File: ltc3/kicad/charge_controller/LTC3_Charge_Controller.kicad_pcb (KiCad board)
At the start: 4 copper layers, 102 x 83 mm, 394 parts, among them P1 MicroFit header, P2 MicroFit header, P3 JST XH header, P4 MicroFit header, P5 JST XH header, P6 JST XH header, Q1 ZVN4525E6, Q2 BSC028N06NS, Q3 BSC028N06NS, Q4 BSC028N06NS, Q5 BSC028N06NS, Q6 ZVP3310F, Q7 MMBT5550L, U1 PI2127, U2 PI2127, U3 LT8490, U4 LTC2990

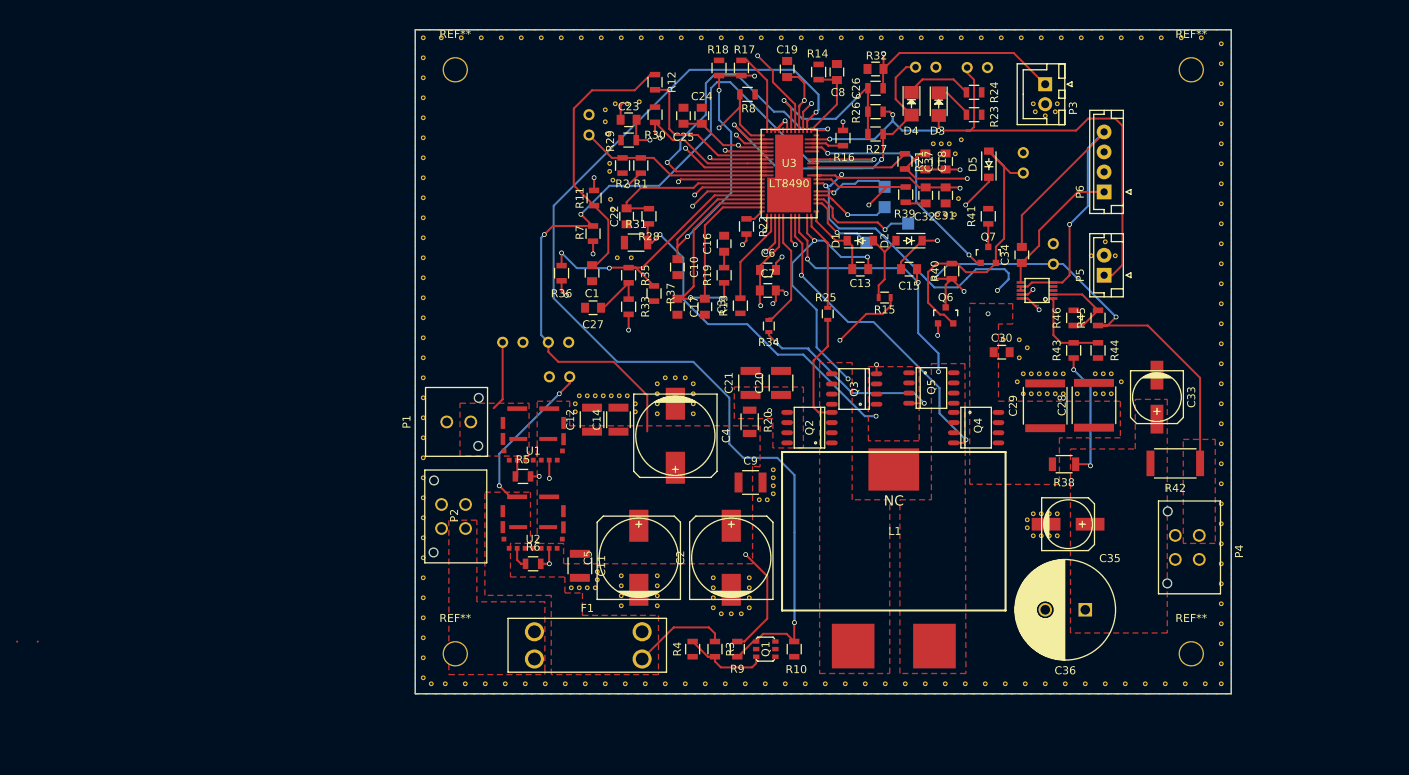
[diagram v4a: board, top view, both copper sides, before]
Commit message: LTC3 Layout Changes to Charge Controller/Cell Balancing
Finished up some changes on charge controller/cell balancing layout.
DRC gives zero errors, and everything is connected, huzzah!
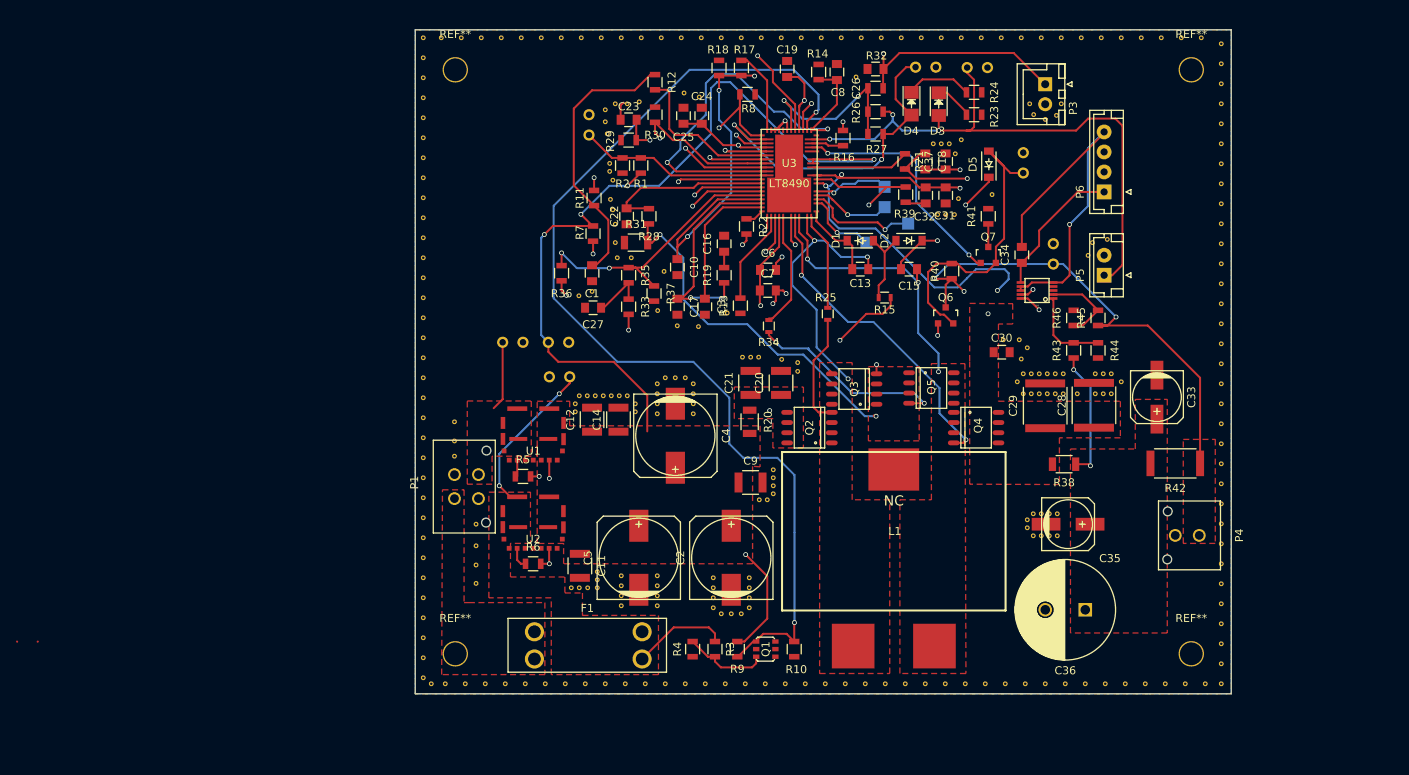
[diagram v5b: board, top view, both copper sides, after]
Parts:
- removed P2: MicroFit header, Connectors_Molex:Molex_Microfit3_Header_02x02_Straight_43045-0428
- removed the REF** at (171.2, 136.0)
- added REF**: Via_.6mm, LTC3:Via_.6mm, F.Cu at (164.6, 82.4)
- added REF**: Via_.6mm, LTC3:Via_.6mm, F.Cu at (122.8, 96.9)
- added REF**: Via_.6mm, LTC3:Via_.6mm, F.Cu at (125.2, 98.8)
- added REF**: Via_.6mm, LTC3:Via_.6mm, F.Cu at (127.9, 98.9)
- added REF**: Via_.6mm, LTC3:Via_.6mm, F.Cu at (131.5, 97.2)
- added REF**: Via_.6mm, LTC3:Via_.6mm, F.Cu at (138.3, 103.0)
- added REF**: Via_.6mm, LTC3:Via_.6mm, F.Cu at (140.3, 103.4)
- added REF**: Via_.6mm, LTC3:Via_.6mm, F.Cu at (140.3, 104.5)
- added REF**: Via_.6mm, LTC3:Via_.6mm, F.Cu at (133.4, 102.7)
- added REF**: Via_.6mm, LTC3:Via_.6mm, F.Cu at (135.4, 102.7)
- added REF**: Via_.6mm, LTC3:Via_.6mm, F.Cu at (134.4, 102.7)
- added REF**: Via_.6mm, LTC3:Via_.6mm, F.Cu at (147.6, 67.7)
- added REF**: Via_.6mm, LTC3:Via_.6mm, F.Cu at (97.4, 110.8)
- added REF**: Via_.6mm, LTC3:Via_.6mm, F.Cu at (97.4, 113.2)
- added REF**: Via_.6mm, LTC3:Via_.6mm, F.Cu at (97.4, 115.1)
- added REF**: Via_.6mm, LTC3:Via_.6mm, F.Cu at (100.1, 123.6)
- added REF**: Via_.6mm, LTC3:Via_.6mm, F.Cu at (100.1, 131.0)
- added REF**: Via_.6mm, LTC3:Via_.6mm, F.Cu at (100.1, 128.7)
- added REF**: Via_.6mm, LTC3:Via_.6mm, F.Cu at (100.1, 126.3)
- added REF**: Via_.6mm, LTC3:Via_.6mm, F.Cu at (128.0, 70.2)
- added REF**: Via_.6mm, LTC3:Via_.6mm, F.Cu at (126.1, 69.7)
- added REF**: Via_.6mm, LTC3:Via_.6mm, F.Cu at (123.6, 92.0)
- added REF**: Via_.6mm, LTC3:Via_.6mm, F.Cu at (117.5, 88.4)
- added REF**: Via_.6mm, LTC3:Via_.6mm, F.Cu at (117.5, 86.1)
- added REF**: Via_.6mm, LTC3:Via_.6mm, F.Cu at (114.6, 94.5)
- added REF**: Via_.6mm, LTC3:Via_.6mm, F.Cu at (171.3, 136.2)
- added REF**: Via_.6mm, LTC3:Via_.6mm, F.Cu at (112.9, 95.0)
- C1: value 0.33u -> 0.33μ
- C10, C8: value 0.01u -> 0.01μ
- C11, C12, C14, C20, C21, C9: value 2.2u -> 2.2μ
- C2, C4, C5: value 33u -> 33μ
- C22, C23: value 0.001u -> 0.001μ
- C24, C28, C29, C6, C7: value 4.7u -> 4.7μ
- C25, C30: value 1u -> 1μ
- C26, C3, C31, C34, C37: value 0.1u -> 0.1μ
- C27: value 0.18u -> 0.18μ
- C33, C35: value 10u -> 10μ
- C36: value 150u -> 150μ
- P1: footprint Connectors_Molex:Molex_Microfit3_Header_02x01_Straight_43045-0228 -> Connectors_Molex:Molex_Microfit3_Header_02x02_Straight_43045-0428
- P3, P5, P6: value JST XH header -> XH header
- P4: footprint Connectors_Molex:Molex_Microfit3_Header_02x02_Straight_43045-0428 -> Connectors_Molex:Molex_Microfit3_Header_02x01_Straight_43045-0228
- moved P1 9.63 mm to (97.4, 120.4)
- moved REF** 3.29 mm to (177.1, 88.4)
- moved REF** 0.50 mm to (173.2, 71.0)
- moved REF** 0.47 mm to (172.6, 72.5)
- moved REF** 0.45 mm to (173.2, 134.2)
- moved REF** 0.45 mm to (171.2, 132.3)
- moved REF** 0.45 mm to (171.2, 73.0)
- moved REF** 0.45 mm to (169.3, 71.0)
- moved REF** 0.45 mm to (169.3, 134.3)
- moved REF** 0.40 mm to (169.8, 72.4)
- moved REF** 0.40 mm to (176.6, 90.0)
- moved REF** 0.39 mm to (179.0, 88.0)
- moved REF** 0.29 mm to (168.2, 102.9)
- moved REF** 0.25 mm to (172.7, 132.9)
- moved REF** 0.25 mm to (115.2, 131.5)
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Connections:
- F1 pad 1: Net-(F1-Pad1) -> /LAB_IN
- P1 pad 1: GND -> /LAB_IN
- P1 pad 2: Net-(P1-Pad2) -> GND
- U1 pad 12: Net-(P1-Pad2) -> /PV_IN
- U1 pad 13: Net-(P1-Pad2) -> /PV_IN
- U1 pad 14: Net-(P1-Pad2) -> /PV_IN
- U1 pad 15: Net-(P1-Pad2) -> /PV_IN
- U1 pad 16: Net-(P1-Pad2) -> /PV_IN
- W3 pad 1: Net-(P1-Pad2) -> /PV_IN
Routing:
- net Net-(P1-Pad2): track 8.70 -> 0.00 mm
- net /PV_IN: track 0.00 -> 8.70 mm
- added copper zone on F.Cu, net /LAB_IN
- added copper zone on F.Cu, net /PV_IN
- removed copper zone on F.Cu, net Net-(F1-Pad1)
- removed copper zone on F.Cu, net Net-(P1-Pad2)

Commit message: LTC3 Layout
Minor changes to charge controller PCB.
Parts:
- added REF**: Via_.6mm, LTC3:Via_.6mm, F.Cu at (164.7, 72.8)
- added REF**: Via_.6mm, LTC3:Via_.6mm, F.Cu at (164.7, 71.8)
- added REF**: Via_.6mm, LTC3:Via_.6mm, F.Cu at (164.7, 70.2)
- added REF**: Via_.6mm, LTC3:Via_.6mm, F.Cu at (164.7, 69.1)
- added REF**: Via_.6mm, LTC3:Via_.6mm, F.Cu at (186.9, 103.4)
- added REF**: Via_.6mm, LTC3:Via_.6mm, F.Cu at (183.3, 103.4)
- added REF**: Via_.6mm, LTC3:Via_.6mm, F.Cu at (186.9, 104.9)
- added REF**: Via_.6mm, LTC3:Via_.6mm, F.Cu at (185.2, 102.0)
- added REF**: Via_.6mm, LTC3:Via_.6mm, F.Cu at (183.3, 104.9)
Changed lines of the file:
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@@
 (kicad_pcb (version 4) (host pcbnew "(2016-05-27 BZR 6836, Git 4441a4b)-product")
   (general
-    (links 572)
+    (links 581)
     (no_connects 0)
-    (area 92.405999 61.725999 194.506001 144.826001)
+    (area 42.423199 60.5199 199.831029 145.9171)
     (thickness 1.6)
     (drawings 4)
     (tracks 824)
     (zones 0)
-    (modules 419)
+    (modules 428)
     (nets 68)
   )
@@
     (1 Ground.Plane signal hide)
     (2 In2.Cu signal)
-    (31 B.Cu signal)
+    (31 B.Cu signal hide)
     (32 B.Adhes user hide)
     (33 F.Adhes user)
@@
   )
   (module LTC3:Via_.6mm (layer F.Cu)
+    (at 164.656 72.826)
+    (fp_text reference REF** (at 0 1.27) (layer F.SilkS) hide
+      (effects (font (size 1 1) (thickness 0.15)))
+    )
+    (fp_text value Via_.6mm (at 0 -1.27) (layer F.Fab) hide
+      (effects (font (size 1 1) (thickness 0.15)))
+    )
+    (pad 1 thru_hole circle (at 0 0) (size 0.6 0.6) (drill 0.3) (layers *.Cu)
+      (net 2 GND) (zone_connect 2))
+  )
+  (module LTC3:Via_.6mm (layer F.Cu)
+    (at 164.656 71.751)
+    (fp_text reference REF** (at 0 1.27) (layer F.SilkS) hide
+      (effects (font (size 1 1) (thickness 0.15)))
+    )
+    (fp_text value Via_.6mm (at 0 -1.27) (layer F.Fab) hide
+      (effects (font (size 1 1) (thickness 0.15)))
+    )
+    (pad 1 thru_hole circle (at 0 0) (size 0.6 0.6) (drill 0.3) (layers *.Cu)
+      (net 2 GND) (zone_connect 2))
+  )
+  (module LTC3:Via_.6mm (layer F.Cu)
+    (at 164.681 70.151)
+    (fp_text reference REF** (at 0 1.27) (layer F.SilkS) hide
+      (effects (font (size 1 1) (thickness 0.15)))
+    )
+    (fp_text value Via_.6mm (at 0 -1.27) (layer F.Fab) hide
+      (effects (font (size 1 1) (thickness 0.15)))
+    )
+    (pad 1 thru_hole circle (at 0 0) (size 0.6 0.6) (drill 0.3) (layers *.Cu)
+      (net 2 GND) (zone_connect 2))
+  )
+  (module LTC3:Via_.6mm (layer F.Cu)
+    (at 164.681 69.076)
+    (fp_text reference REF** (at 0 1.27) (layer F.SilkS) hide
+      (effects (font (size 1 1) (thickness 0.15)))
+    )
+    (fp_text value Via_.6mm (at 0 -1.27) (layer F.Fab) hide
+      (effects (font (size 1 1) (thickness 0.15)))
+    )
+    (pad 1 thru_hole circle (at 0 0) (size 0.6 0.6) (drill 0.3) (layers *.Cu)
+      (net 2 GND) (zone_connect 2))
+  )
+  (module LTC3:Via_.6mm (layer F.Cu)
+    (at 186.931 103.426)
+    (fp_text reference REF** (at 0 1.27) (layer F.SilkS) hide
+      (effects (font (size 1 1) (thickness 0.15)))
+    )
+    (fp_text value Via_.6mm (at 0 -1.27) (layer F.Fab) hide
+      (effects (font (size 1 1) (thickness 0.15)))
+    )
+    (pad 1 thru_hole circle (at 0 0) (size 0.6 0.6) (drill 0.3) (layers *.Cu)
+      (net 2 GND) (zone_connect 2))
+  )
+  (module LTC3:Via_.6mm (layer F.Cu)
+    (at 183.331 103.426)
+    (fp_text reference REF** (at 0 1.27) (layer F.SilkS) hide
+      (effects (font (size 1 1) (thickness 0.15)))
+    )
+    (fp_text value Via_.6mm (at 0 -1.27) (layer F.Fab) hide
+      (effects (font (size 1 1) (thickness 0.15)))
+    )
+    (pad 1 thru_hole circle (at 0 0) (size 0.6 0.6) (drill 0.3) (layers *.Cu)
+      (net 2 GND) (zone_connect 2))
+  )
+  (module LTC3:Via_.6mm (layer F.Cu)
+    (at 186.931 104.901)
+    (fp_text reference REF** (at 0 1.27) (layer F.SilkS) hide
+      (effects (font (size 1 1) (thickness 0.15)))
+    )
+    (fp_text value Via_.6mm (at 0 -1.27) (layer F.Fab) hide
+      (effects (font (size 1 1) (thickness 0.15)))
+    )
+    (pad 1 thru_hole circle (at 0 0) (size 0.6 0.6) (drill 0.3) (layers *.Cu)
+      (net 2 GND) (zone_connect 2))
+  )
+  (module LTC3:Via_.6mm (layer F.Cu)
+    (at 185.156 101.976)
+    (fp_text reference REF** (at 0 1.27) (layer F.SilkS) hide
+      (effects (font (size 1 1) (thickness 0.15)))
+    )
+    (fp_text value Via_.6mm (at 0 -1.27) (layer F.Fab) hide
+      (effects (font (size 1 1) (thickness 0.15)))
+    )
+    (pad 1 thru_hole circle (at 0 0) (size 0.6 0.6) (drill 0.3) (layers *.Cu)
+      (net 2 GND) (zone_connect 2))
+  )
+  (module LTC3:Via_.6mm (layer F.Cu)
+    (at 183.331 104.901)
+    (fp_text reference REF** (at 0 1.27) (layer F.SilkS) hide
+      (effects (font (size 1 1) (thickness 0.15)))
+    )
+    (fp_text value Via_.6mm (at 0 -1.27) (layer F.Fab) hide
+      (effects (font (size 1 1) (thickness 0.15)))
+    )
+    (pad 1 thru_hole circle (at 0 0) (size 0.6 0.6) (drill 0.3) (layers *.Cu)
+      (net 2 GND) (zone_connect 2))
+  )
+  (module LTC3:Via_.6mm (layer F.Cu)

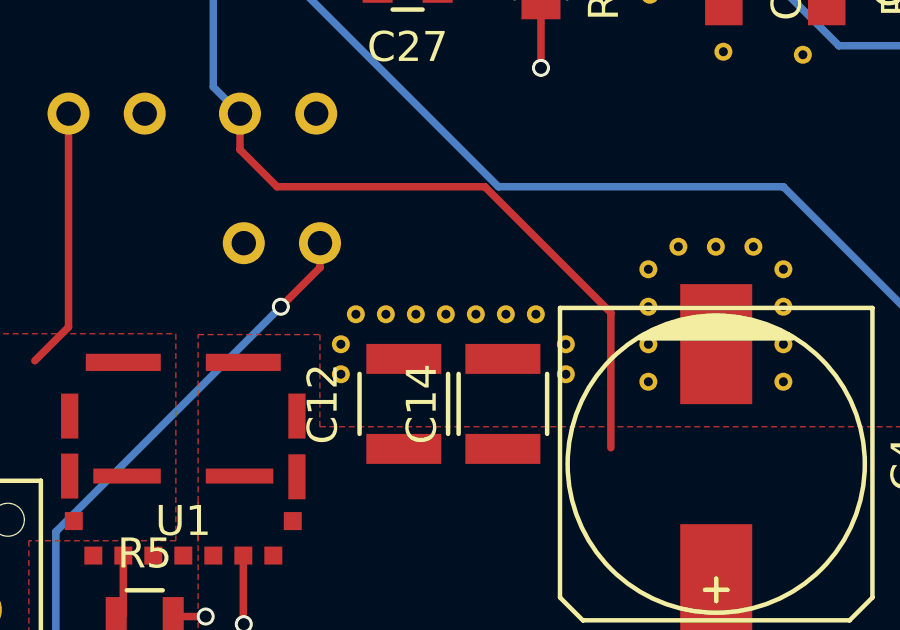
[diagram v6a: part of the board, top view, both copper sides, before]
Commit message: LTC3: Last Minute Layout Stuff
Some last minute changes on the charge controller/cell protection board.
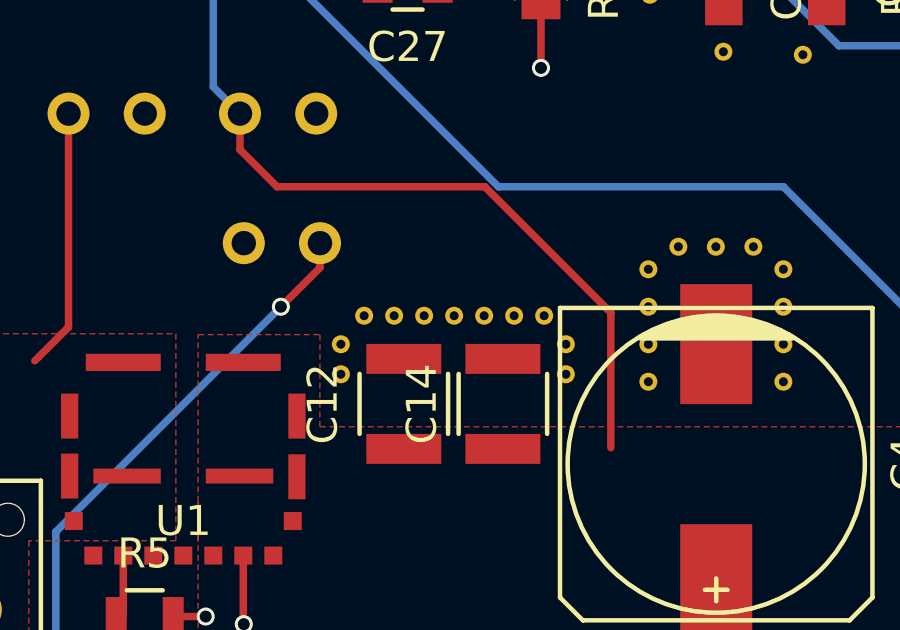
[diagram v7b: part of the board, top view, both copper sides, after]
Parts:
- moved REF** 0.28 mm to (113.2, 107.6)
- moved REF** 0.28 mm to (114.2, 107.6)
- moved REF** 0.28 mm to (115.2, 107.6)
- moved REF** 0.28 mm to (116.2, 107.6)
- moved REF** 0.28 mm to (117.2, 107.6)
- moved REF** 0.28 mm to (118.2, 107.6)
- moved REF** 0.28 mm to (119.2, 107.6)
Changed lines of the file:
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@@
     (0 F.Cu signal)
     (1 Ground.Plane signal hide)
-    (2 In2.Cu signal)
+    (2 In2.Cu signal hide)
     (31 B.Cu signal hide)
     (32 B.Adhes user hide)
@@
   )
   (module LTC3:Via_.6mm (layer F.Cu)
-    (at 112.956 107.526)
-    (fp_text reference REF** (at 0 1.27) (layer F.SilkS) hide
-      (effects (font (size 1 1) (thickness 0.15)))
-    )
-    (fp_text value Via_.6mm (at 0 -1.27) (layer F.Fab) hide
-      (effects (font (size 1 1) (thickness 0.15)))
-    )
-    (pad 1 thru_hole circle (at 0 0) (size 0.6 0.6) (drill 0.3) (layers *.Cu)
-      (net 2 GND) (zone_connect 2))
-  )
-  (module LTC3:Via_.6mm (layer F.Cu)
-    (at 113.956 107.526)
-    (fp_text reference REF** (at 0 1.27) (layer F.SilkS) hide
-      (effects (font (size 1 1) (thickness 0.15)))
-    )
-    (fp_text value Via_.6mm (at 0 -1.27) (layer F.Fab) hide
-      (effects (font (size 1 1) (thickness 0.15)))
-    )
-    (pad 1 thru_hole circle (at 0 0) (size 0.6 0.6) (drill 0.3) (layers *.Cu)
-      (net 2 GND) (zone_connect 2))
-  )
-  (module LTC3:Via_.6mm (layer F.Cu)
-    (at 114.956 107.526)
-    (fp_text reference REF** (at 0 1.27) (layer F.SilkS) hide
-      (effects (font (size 1 1) (thickness 0.15)))
-    )
-    (fp_text value Via_.6mm (at 0 -1.27) (layer F.Fab) hide
-      (effects (font (size 1 1) (thickness 0.15)))
-    )
-    (pad 1 thru_hole circle (at 0 0) (size 0.6 0.6) (drill 0.3) (layers *.Cu)
-      (net 2 GND) (zone_connect 2))
-  )
-  (module LTC3:Via_.6mm (layer F.Cu)
-    (at 115.956 107.526)
-    (fp_text reference REF** (at 0 1.27) (layer F.SilkS) hide
-      (effects (font (size 1 1) (thickness 0.15)))
-    )
-    (fp_text value Via_.6mm (at 0 -1.27) (layer F.Fab) hide
-      (effects (font (size 1 1) (thickness 0.15)))
-    )
-    (pad 1 thru_hole circle (at 0 0) (size 0.6 0.6) (drill 0.3) (layers *.Cu)
-      (net 2 GND) (zone_connect 2))
-  )
-  (module LTC3:Via_.6mm (layer F.Cu)
-    (at 116.956 107.526)
-    (fp_text reference REF** (at 0 1.27) (layer F.SilkS) hide
-      (effects (font (size 1 1) (thickness 0.15)))
-    )
-    (fp_text value Via_.6mm (at 0 -1.27) (layer F.Fab) hide
-      (effects (font (size 1 1) (thickness 0.15)))
-    )
-    (pad 1 thru_hole circle (at 0 0) (size 0.6 0.6) (drill 0.3) (layers *.Cu)
-      (net 2 GND) (zone_connect 2))
-  )
-  (module LTC3:Via_.6mm (layer F.Cu)
-    (at 117.956 107.526)
-    (fp_text reference REF** (at 0 1.27) (layer F.SilkS) hide
-      (effects (font (size 1 1) (thickness 0.15)))
-    )
-    (fp_text value Via_.6mm (at 0 -1.27) (layer F.Fab) hide
-      (effects (font (size 1 1) (thickness 0.15)))
-    )
-    (pad 1 thru_hole circle (at 0 0) (size 0.6 0.6) (drill 0.3) (layers *.Cu)
-      (net 2 GND) (zone_connect 2))
-  )
-  (module LTC3:Via_.6mm (layer F.Cu)
-    (at 118.956 107.526)
+    (at 113.231 107.576)
+    (fp_text reference REF** (at 0 1.27) (layer F.SilkS) hide
+      (effects (font (size 1 1) (thickness 0.15)))
+    )
+    (fp_text value Via_.6mm (at 0 -1.27) (layer F.Fab) hide
+      (effects (font (size 1 1) (thickness 0.15)))
+    )
+    (pad 1 thru_hole circle (at 0 0) (size 0.6 0.6) (drill 0.3) (layers *.Cu)
+      (net 2 GND) (zone_connect 2))
+  )
+  (module LTC3:Via_.6mm (layer F.Cu)
+    (at 114.231 107.576)
+    (fp_text reference REF** (at 0 1.27) (layer F.SilkS) hide
+      (effects (font (size 1 1) (thickness 0.15)))
+    )
+    (fp_text value Via_.6mm (at 0 -1.27) (layer F.Fab) hide
+      (effects (font (size 1 1) (thickness 0.15)))
+    )
+    (pad 1 thru_hole circle (at 0 0) (size 0.6 0.6) (drill 0.3) (layers *.Cu)
+      (net 2 GND) (zone_connect 2))
+  )
+  (module LTC3:Via_.6mm (layer F.Cu)
+    (at 115.231 107.576)
+    (fp_text reference REF** (at 0 1.27) (layer F.SilkS) hide
+      (effects (font (size 1 1) (thickness 0.15)))
+    )
+    (fp_text value Via_.6mm (at 0 -1.27) (layer F.Fab) hide
+      (effects (font (size 1 1) (thickness 0.15)))
+    )
+    (pad 1 thru_hole circle (at 0 0) (size 0.6 0.6) (drill 0.3) (layers *.Cu)
+      (net 2 GND) (zone_connect 2))
+  )
+  (module LTC3:Via_.6mm (layer F.Cu)
+    (at 116.231 107.576)
+    (fp_text reference REF** (at 0 1.27) (layer F.SilkS) hide
+      (effects (font (size 1 1) (thickness 0.15)))
+    )
+    (fp_text value Via_.6mm (at 0 -1.27) (layer F.Fab) hide
+      (effects (font (size 1 1) (thickness 0.15)))
+    )
+    (pad 1 thru_hole circle (at 0 0) (size 0.6 0.6) (drill 0.3) (layers *.Cu)
+      (net 2 GND) (zone_connect 2))
+  )
+  (module LTC3:Via_.6mm (layer F.Cu)
+    (at 117.231 107.576)
+    (fp_text reference REF** (at 0 1.27) (layer F.SilkS) hide
+      (effects (font (size 1 1) (thickness 0.15)))
+    )
+    (fp_text value Via_.6mm (at 0 -1.27) (layer F.Fab) hide
+      (effects (font (size 1 1) (thickness 0.15)))
+    )
+    (pad 1 thru_hole circle (at 0 0) (size 0.6 0.6) (drill 0.3) (layers *.Cu)
+      (net 2 GND) (zone_connect 2))
+  )
+  (module LTC3:Via_.6mm (layer F.Cu)
+    (at 118.231 107.576)
+    (fp_text reference REF** (at 0 1.27) (layer F.SilkS) hide
+      (effects (font (size 1 1) (thickness 0.15)))
+    )
+    (fp_text value Via_.6mm (at 0 -1.27) (layer F.Fab) hide
+      (effects (font (size 1 1) (thickness 0.15)))
+    )
+    (pad 1 thru_hole circle (at 0 0) (size 0.6 0.6) (drill 0.3) (layers *.Cu)
+      (net 2 GND) (zone_connect 2))
+  )
+  (module LTC3:Via_.6mm (layer F.Cu)
+    (at 119.231 107.576)
     (fp_text reference REF** (at 0 0) (layer F.SilkS) hide
       (effects (font (size 1 1) (thickness 0.15)))
